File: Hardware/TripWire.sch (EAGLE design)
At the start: 56 parts, among them P1 LSP11, P2 LSP11, P3 LSP11, P4 LSP11, P5 LSP11, P6 LSP11, P7 LSP11, X1 GADGETEER-SOCKET

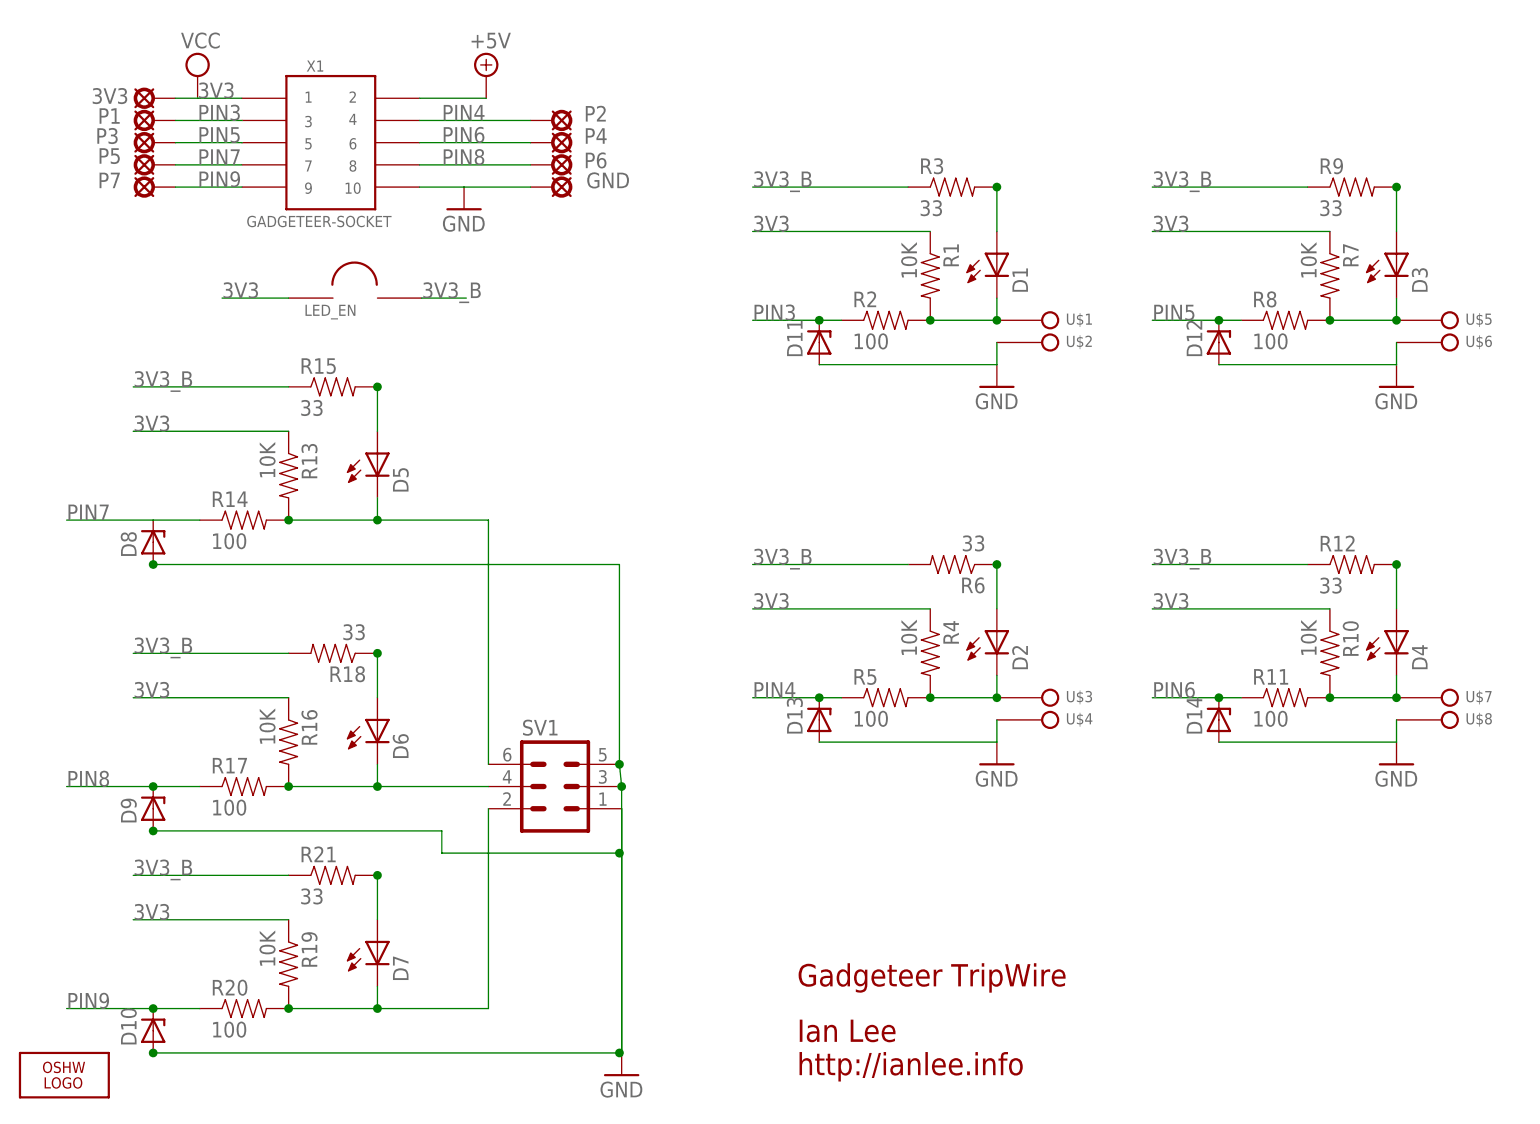
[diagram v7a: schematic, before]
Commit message: WiP - adding TVS diode array.
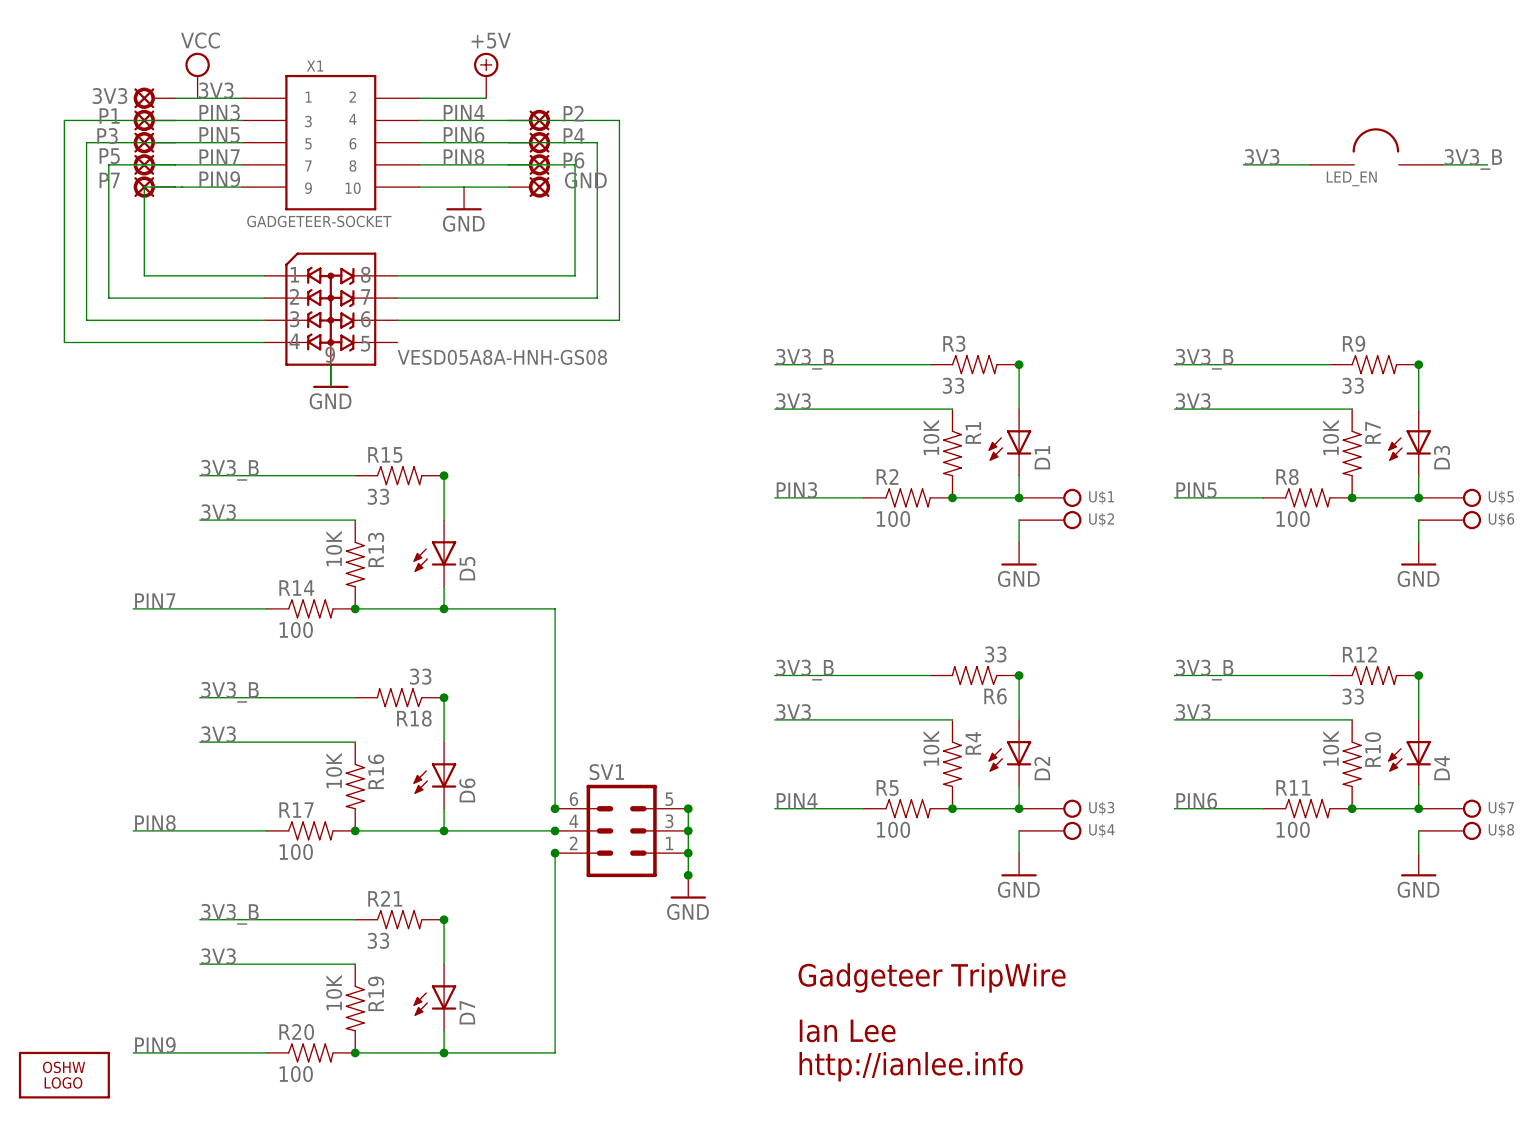
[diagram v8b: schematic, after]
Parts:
- removed D10, D11, D12, D13, D14, D8, D9: (no value), diode:ZENER-DIODESOD80C
- added VESD05A8A-HNH-GS08: VESD05A8A-HNH-GS088-UFDFN_TVS-DIODE-ARRAY, SoftDust:VESD05A8A-HNH-GS088-UFDFN_TVS-DIODE-ARRAY
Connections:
- removed net N$15: D9.A
- removed net N$16: D10.A
- net GND: now also VESD05A8A-HNH-GS08.P$9; no longer D11.A, D12.A, D13.A, D14.A, D8.A
- net PIN3: now also VESD05A8A-HNH-GS08.P$4; no longer D11.C
- net PIN4: now also VESD05A8A-HNH-GS08.P$6; no longer D13.C
- net PIN5: now also VESD05A8A-HNH-GS08.P$3; no longer D12.C
- net PIN6: now also VESD05A8A-HNH-GS08.P$7; no longer D14.C
- net PIN7: now also VESD05A8A-HNH-GS08.P$2; no longer D8.C
- net PIN8: now also VESD05A8A-HNH-GS08.P$8; no longer D9.C
- net PIN9: now also VESD05A8A-HNH-GS08.P$1; no longer D10.C
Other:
- moved on the sheet: D1, D2, D3, D4, D5, D6, D7, GND, LED_EN, P2, P4, P6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
